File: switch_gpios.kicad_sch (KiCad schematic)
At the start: 29 parts

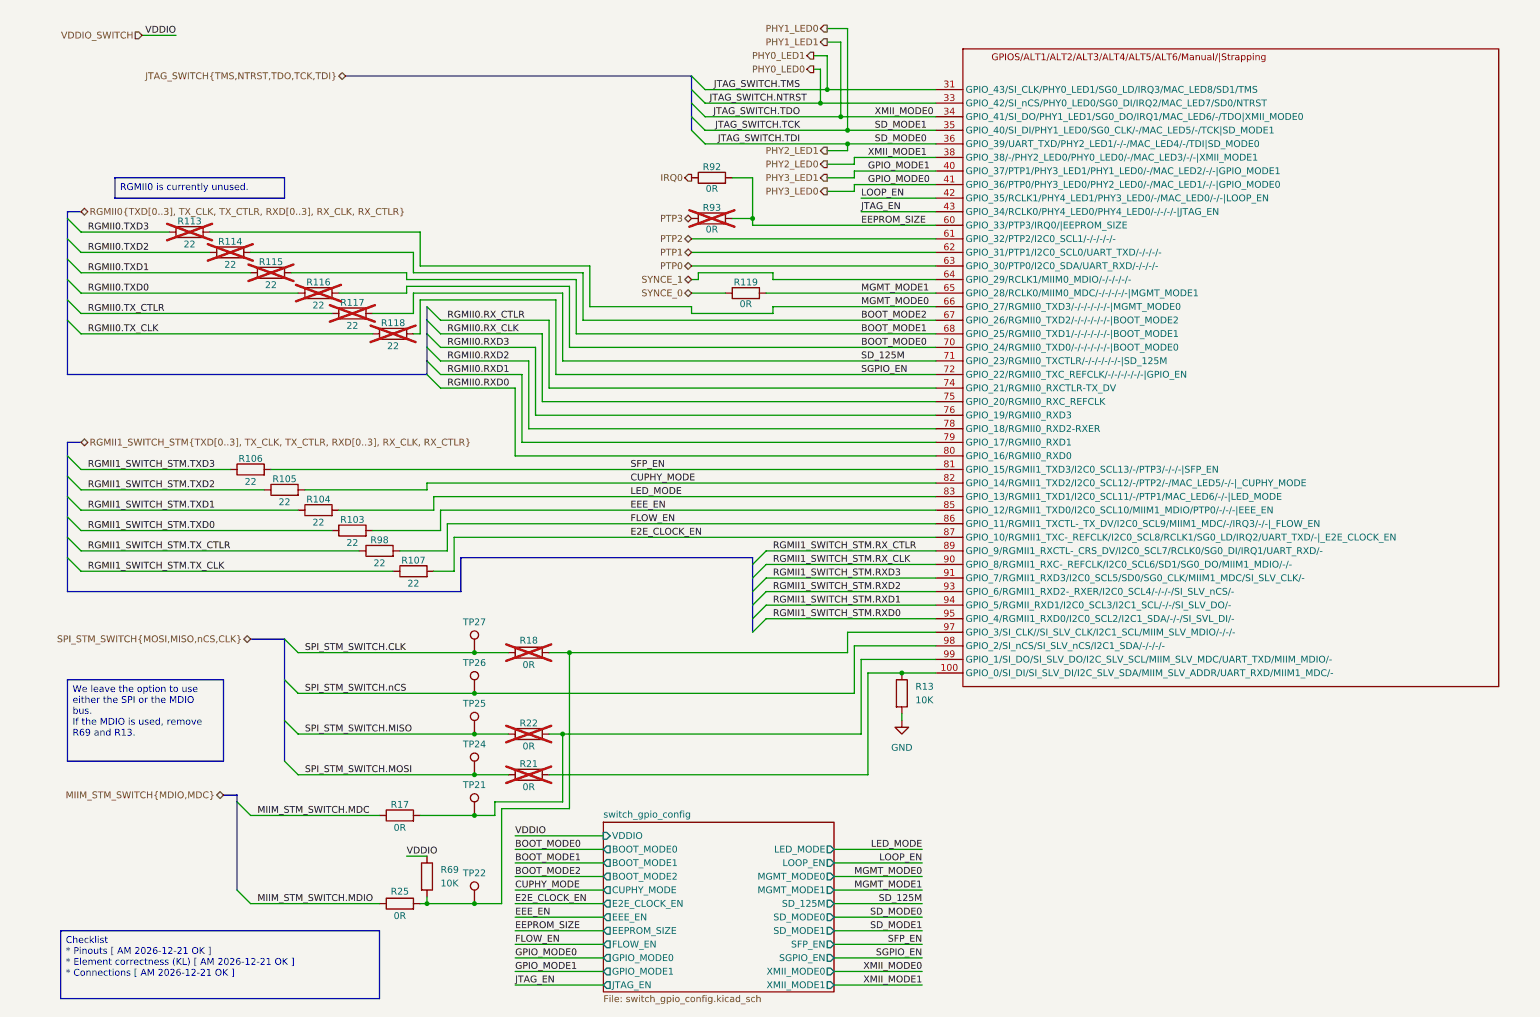
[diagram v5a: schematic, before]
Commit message: updates components from my library misconfiguration. Refs: #1
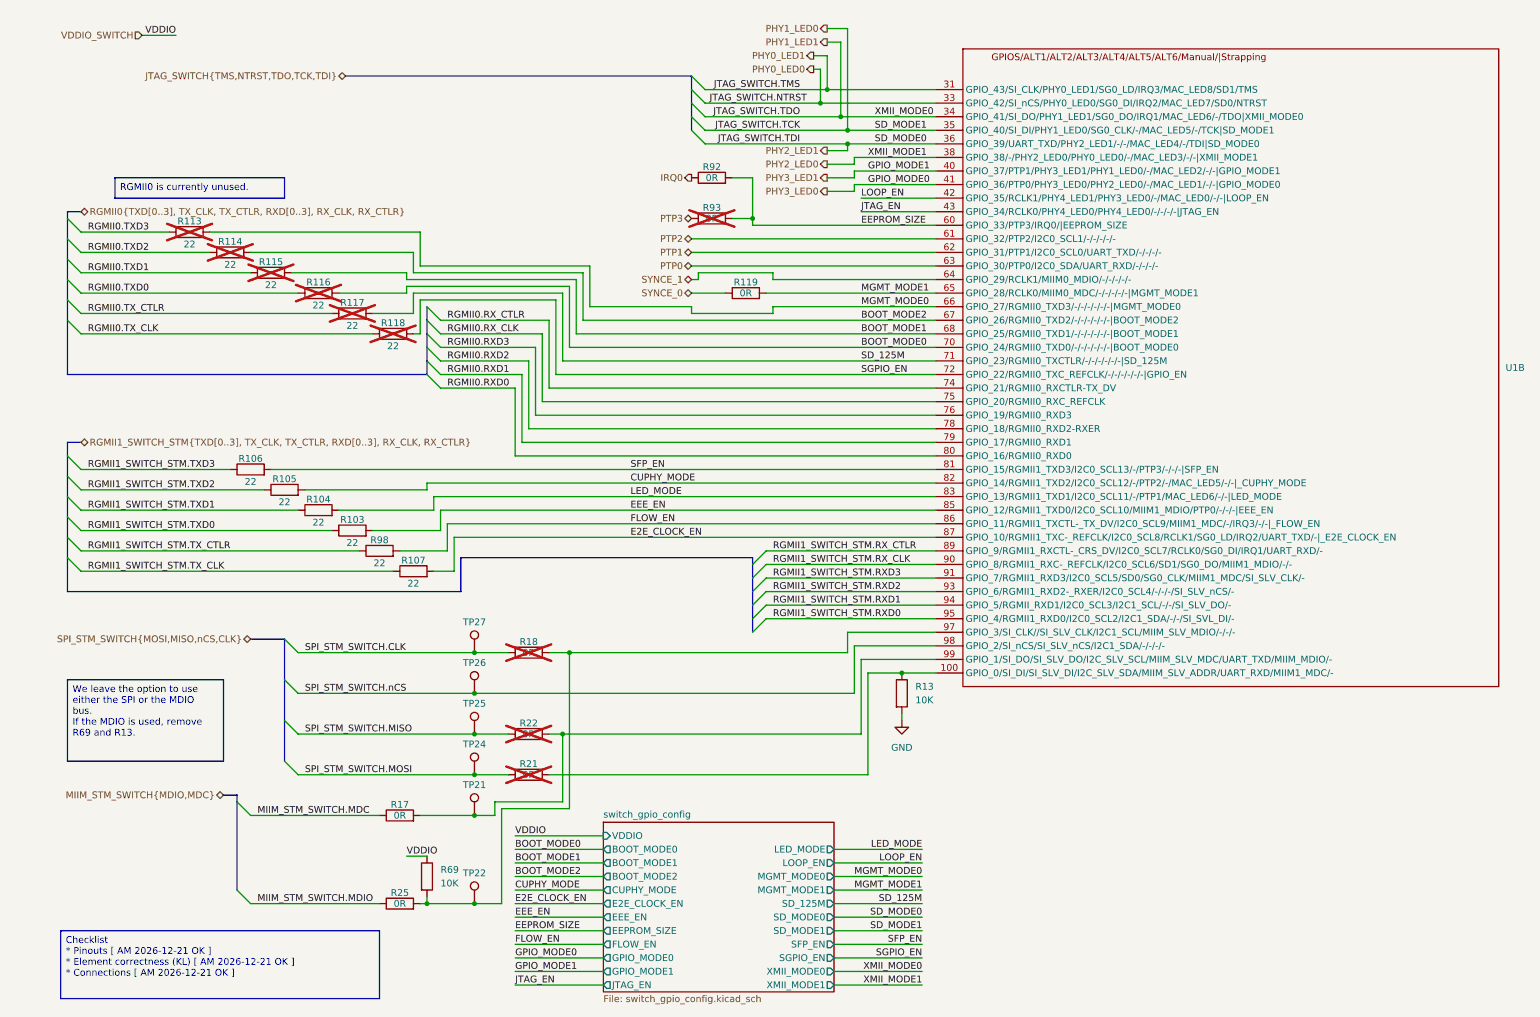
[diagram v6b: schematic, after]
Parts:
- R17, R25, R92: footprint KL_Footprints:C_0603 -> KL_Footprints:R_0603
- R18, R21, R22, R93: footprint KL_Footprints:C_0603 -> KL_Footprints:R_0603; now in the parts list
- U1: footprint Package_QFP:TQFP-128_14x14mm_P0.4mm -> KL_Footprints:TQFP-128_14x14mm_P0.4mm
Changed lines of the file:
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@@
 		)
 		(property "Value" "0R"
-			(at 135.89 45.212 90)
-			(effects
-				(font
-					(size 1.27 1.27)
-				)
-			)
-		)
-		(property "Footprint" "KL_Footprints:C_0603"
+			(at 135.89 43.18 90)
+			(effects
+				(font
+					(size 1.27 1.27)
+				)
+			)
+		)
+		(property "Footprint" "KL_Footprints:R_0603"
 			(at 135.89 44.958 90)
 			(effects
@@
 	)
 	(symbol
-		(lib_name "R_0R_250mW_0.5_0603_1")
 		(lib_id "KL_R:R_0R_250mW_0.5_0603")
 		(at 142.24 64.77 90)
@@
 		)
 		(property "Value" "0R"
-			(at 142.24 66.802 90)
+			(at 142.24 64.77 90)
 			(effects
 				(font
@@
 		)
 		(property "Value" "0R"
-			(at 77.47 164.846 90)
-			(effects
-				(font
-					(size 1.27 1.27)
-				)
-			)
-		)
-		(property "Footprint" "KL_Footprints:C_0603"
+			(at 77.47 162.56 90)
+			(effects
+				(font
+					(size 1.27 1.27)
+				)
+			)
+		)
+		(property "Footprint" "KL_Footprints:R_0603"
 			(at 77.47 164.338 90)
 			(effects
@@
 		(unit 1)
 		(exclude_from_sim no)
-		(in_bom no)
+		(in_bom yes)
 		(on_board yes)
 		(dnp yes)
 		(property "Reference" "R18"
-			(at 101.6 129.794 90)
+			(at 101.6 130.048 90)
 			(effects
 				(font
@@
 		)
 		(property "Value" "0R"
-			(at 101.6 134.366 90)
-			(effects
-				(font
-					(size 1.27 1.27)
-				)
-			)
-		)
-		(property "Footprint" "KL_Footprints:C_0603"
+			(at 101.6 132.08 90)
+			(effects
+				(font
+					(size 1.27 1.27)
+				)
+			)
+		)
+		(property "Footprint" "KL_Footprints:R_0603"
 			(at 101.6 133.858 90)
 			(effects
@@
 		(dnp no)
 		(property "Reference" "R25"
-			(at 77.47 176.784 90)
+			(at 77.47 177.038 90)
 			(effects
 				(font
@@
 		)
 		(property "Value" "0R"
-			(at 77.47 181.356 90)
-			(effects
-				(font
-					(size 1.27 1.27)
-				)
-			)
-		)
-		(property "Footprint" "KL_Footprints:C_0603"
+			(at 77.47 179.07 90)
+			(effects
+				(font
+					(size 1.27 1.27)
+				)
+			)
+		)
+		(property "Footprint" "KL_Footprints:R_0603"
 			(at 77.47 180.848 90)
 			(effects
@@
 		(unit 1)
 		(exclude_from_sim no)
-		(in_bom no)
+		(in_bom yes)
 		(on_board yes)
 		(dnp yes)
@@
 		)
 		(property "Value" "0R"
-			(at 135.89 52.832 90)
-			(effects
-				(font
-					(size 1.27 1.27)
-				)
-			)
-		)
-		(property "Footprint" "KL_Footprints:C_0603"
+			(at 135.89 50.8 90)
+			(effects
+				(font
+					(size 1.27 1.27)
+				)
+			)
+		)
+		(property "Footprint" "KL_Footprints:R_0603"
 			(at 135.89 52.578 90)
 			(effects
@@
 		(unit 1)
 		(exclude_from_sim no)
-		(in_bom no)
+		(in_bom yes)
 		(on_board yes)
 		(dnp yes)
@@
 		)
 		(property "Value" "0R"
-			(at 101.6 149.606 90)
-			(effects
-				(font
-					(size 1.27 1.27)
-				)
-			)
-		)
-		(property "Footprint" "KL_Footprints:C_0603"
+			(at 101.6 147.32 90)
+			(effects
+				(font
+					(size 1.27 1.27)
+				)
+			)
+		)
+		(property "Footprint" "KL_Footprints:R_0603"
 			(at 101.6 149.098 90)
 			(effects
@@
 		(fields_autoplaced yes)
 		(property "Reference" "U1"
-			(at 198.12 13.97 0)
-			(effects
-				(font
-					(size 1.27 1.27)
-				)
-				(hide yes)
+			(at 284.48 78.7399 0)
+			(effects
+				(font
+					(size 1.27 1.27)
+				)
+				(justify left)
 			)
 		)
@@
 					(size 1.27 1.27)
 				)
-			)
-		)
-		(property "Footprint" "Package_QFP:TQFP-128_14x14mm_P0.4mm"
+				(hide yes)
+			)
+		)
+		(property "Footprint" "KL_Footprints:TQFP-128_14x14mm_P0.4mm"
 			(at 198.882 11.938 0)
 			(effects
@@
 		(unit 1)
 		(exclude_from_sim no)
-		(in_bom no)
+		(in_bom yes)
 		(on_board yes)
 		(dnp yes)
@@
 		)
 		(property "Value" "0R"
-			(at 101.6 157.226 90)
-			(effects
-				(font
-					(size 1.27 1.27)
-				)
-			)
-		)
-		(property "Footprint" "KL_Footprints:C_0603"
+			(at 101.6 154.94 90)
+			(effects
+				(font
+					(size 1.27 1.27)
+				)
+			)
+		)
+		(property "Footprint" "KL_Footprints:R_0603"
 			(at 101.6 156.718 90)
 			(effects

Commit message: removes unused busses, adds cheaper 0R resistor, clean up to fix ERC errors. Refs: #1
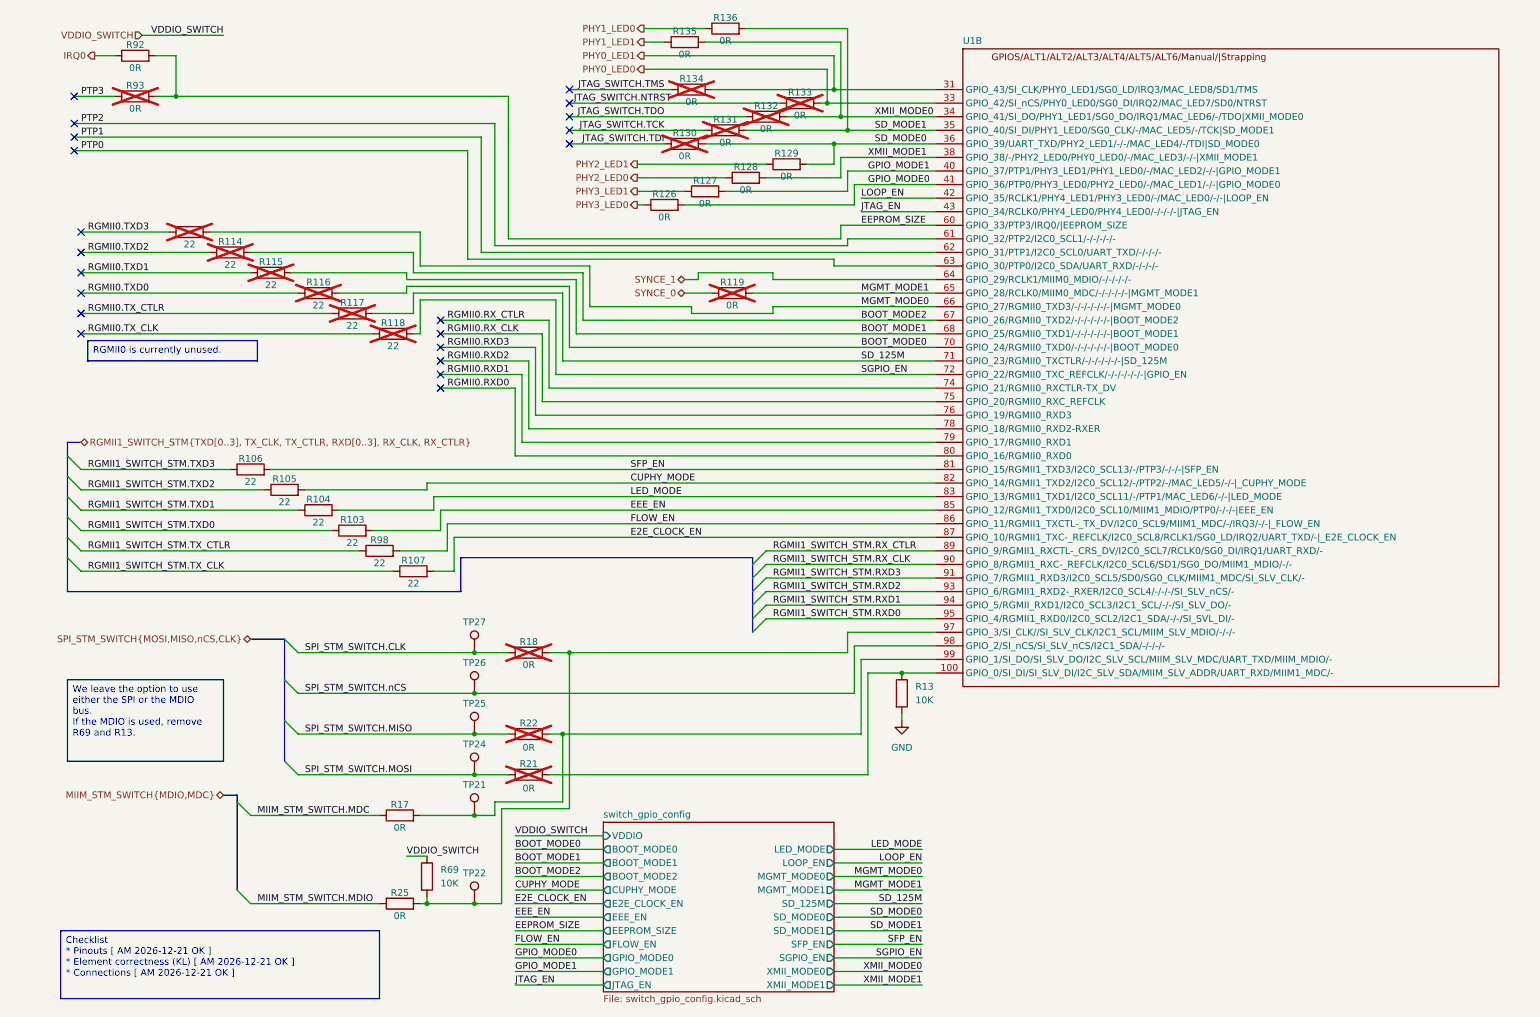
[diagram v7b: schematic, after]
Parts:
- added R126, R127, R128, R129, R130, R131, R132, R133, R134, R135, R136: 0R, KL_Footprints:R_0603, symbol KL_R:R_0R_100mW_5_0603
- R119: symbol KL_R:R_0R_250mW_0.5_0603 -> KL_R:R_0R_100mW_5_0603; Digikey 541-2779-1-ND -> YAG1307CT-ND; Farnell 3235077 -> (none); LCSC C2126552 -> C3017805; Mouser 71-RCS06030000Z0EA -> 603-RC0603JR-070RP; Power 250mW -> 0.1; Tolerance 0.5% -> 5; now not fitted; now left out of the parts list
- R17, R18, R21, R22, R25, R92, R93: symbol KL_R:R_0R_250mW_0.5_0603 -> KL_R:R_0R_100mW_5_0603; Digikey 541-2779-1-ND -> YAG1307CT-ND; Farnell 3235077 -> (none); LCSC C2126552 -> C3017805; Mouser 71-RCS06030000Z0EA -> 603-RC0603JR-070RP; Power 250mW -> 0.1; Tolerance 0.5% -> 5
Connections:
- net PHY0_LED0: now also R133.2
- net PHY0_LED1: now also R134.2
- net PHY1_LED0: now also R136.1; no longer U1.35 (GPIO_40/SI_DI/PHY1_LED0/SG0_CLK/-/MAC_LED5/-/TCK|SD_MODE1)
- net PHY1_LED1: now also R135.1; no longer U1.34 (GPIO_41/SI_DO/PHY1_LED1/SG0_DO/IRQ1/MAC_LED6/-/TDO|XMII_MODE0)
- net PHY2_LED0: now also R128.1; no longer U1.38 (GPIO_38/-/PHY2_LED0/PHY0_LED0/-/MAC_LED3/-/-|XMII_MODE1)
- net PHY2_LED1: now also R129.1; no longer U1.36 (GPIO_39/UART_TXD/PHY2_LED1/-/-/MAC_LED4/-/TDI|SD_MODE0)
- net PHY3_LED0: now also R126.1; no longer U1.41 (GPIO_36/PTP0/PHY3_LED0/PHY2_LED0/-/MAC_LED1/-/-|GPIO_MODE0)
- net PHY3_LED1: now also R127.1; no longer U1.40 (GPIO_37/PTP1/PHY3_LED1/PHY1_LED0/-/MAC_LED2/-/-|GPIO_MODE1)
- new net GPIO_MODE0: R126.2, U1.41 (GPIO_36/PTP0/PHY3_LED0/PHY2_LED0/-/MAC_LED1/-/-|GPIO_MODE0)
- new net GPIO_MODE1: R127.2, U1.40 (GPIO_37/PTP1/PHY3_LED1/PHY1_LED0/-/MAC_LED2/-/-|GPIO_MODE1)
- new net JTAG_SWITCH.NTRST: R133.1
- new net JTAG_SWITCH.TCK: R131.1
- new net JTAG_SWITCH.TDI: R130.1
- new net JTAG_SWITCH.TDO: R132.1
- new net JTAG_SWITCH.TMS: R134.1
- new net SD_MODE0: R129.2, R130.2, U1.36 (GPIO_39/UART_TXD/PHY2_LED1/-/-/MAC_LED4/-/TDI|SD_MODE0)
- new net SD_MODE1: R131.2, R136.2, U1.35 (GPIO_40/SI_DI/PHY1_LED0/SG0_CLK/-/MAC_LED5/-/TCK|SD_MODE1)
- new net XMII_MODE0: R132.2, R135.2, U1.34 (GPIO_41/SI_DO/PHY1_LED1/SG0_DO/IRQ1/MAC_LED6/-/TDO|XMII_MODE0)
- new net XMII_MODE1: R128.2, U1.38 (GPIO_38/-/PHY2_LED0/PHY0_LED0/-/MAC_LED3/-/-|XMII_MODE1)
- no-connect marks 0 -> 21
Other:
- moved on the sheet: R92, R93
